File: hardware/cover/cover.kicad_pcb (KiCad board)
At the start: 2 copper layers, 115 x 35 mm, 10 parts

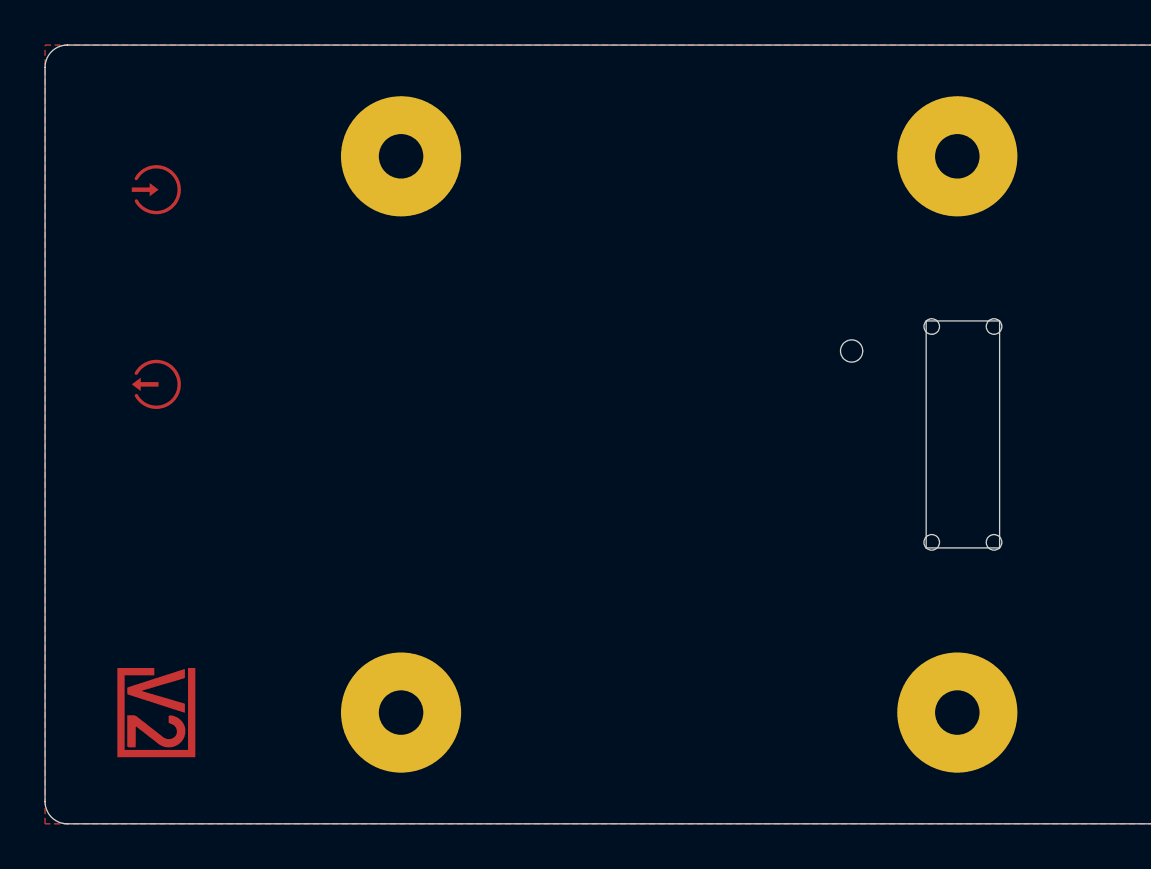
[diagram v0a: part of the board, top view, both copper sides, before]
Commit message: Replace Order_Number
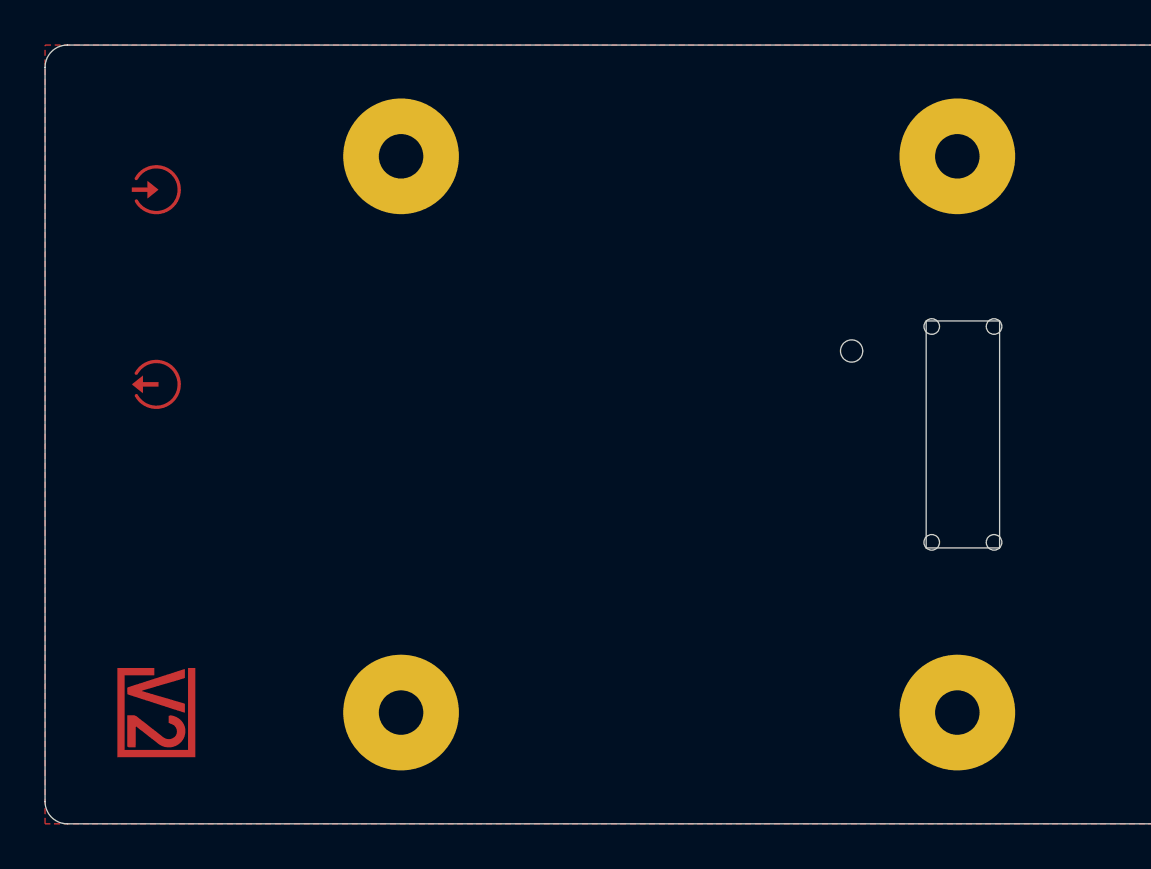
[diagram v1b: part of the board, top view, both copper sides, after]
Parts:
- H101, H102, H103, H104: value MountingHole_2mm_Pad_5.2mm -> 2mm_Pad_5.2mm
- H105: value MountingHole_1mm -> 1mm
- INFO101: value ORDER-NUMBER -> ~; footprint V2_Production:Order_Number -> V2_Production:Revision
